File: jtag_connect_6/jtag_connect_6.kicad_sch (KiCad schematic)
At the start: 2 parts, among them J1 jtag-connect-6, J2 Conn_01x06_Pin

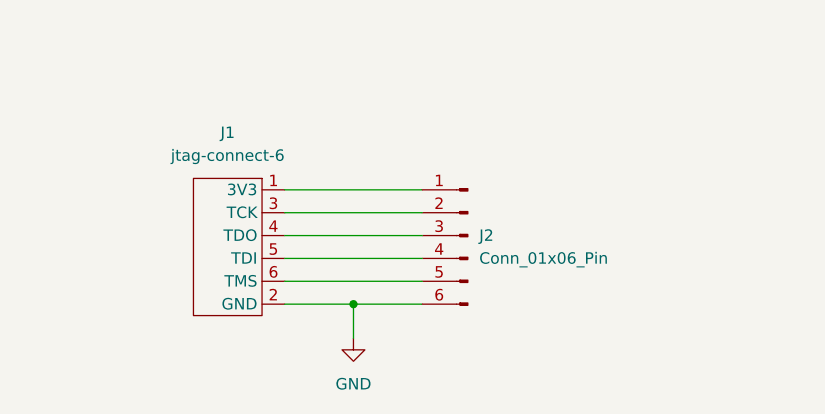
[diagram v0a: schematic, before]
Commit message: Better size and new pins for JTAG
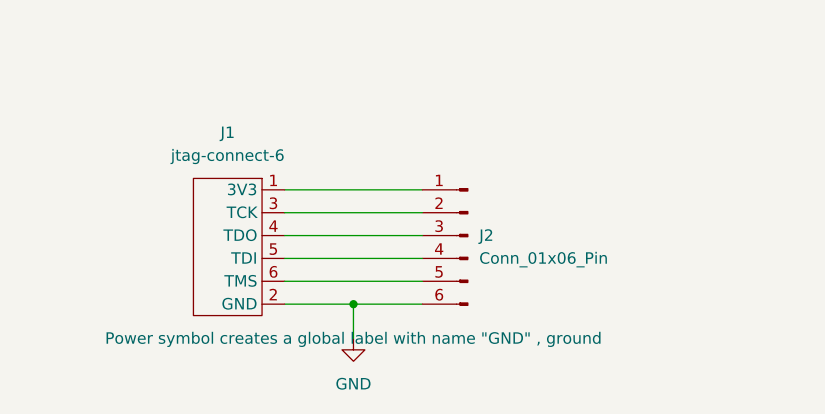
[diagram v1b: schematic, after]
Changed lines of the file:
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@@
 			)
 		)
-		(property "Description" ""
+		(property "Description" "Power symbol creates a global label with name \"GND\" , ground"
 			(at 113.03 105.41 0)
 			(effects

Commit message: Update JTAG to use plated through holes for strength. Also use Sipeed RV Debugger pinout
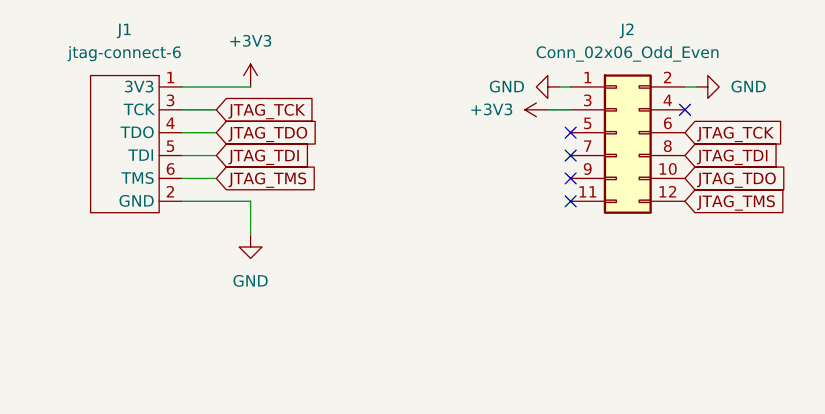
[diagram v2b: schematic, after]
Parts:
- removed J2: Conn_01x06_Pin, Connector_PinHeader_2.54mm:PinHeader_1x06_P2.54mm_Vertical, symbol Connector:Conn_01x06_Pin
- added J2: Conn_02x06_Odd_Even, Connector_PinSocket_2.54mm:PinSocket_2x06_P2.54mm_Vertical, symbol Connector_Generic:Conn_02x06_Odd_Even
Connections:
- net GND: now also J2.1 (Pin_1), J2.2 (Pin_2)
- net +3V3: now reaches J1.1 (3V3)
- net +3V3: now also J2.3 (Pin_3)
- net JTAG_TCK: now reaches J1.3 (TCK)
- net JTAG_TCK: now also J2.6 (Pin_6)
- net JTAG_TDO: now reaches J1.4 (TDO)
- net JTAG_TDO: now also J2.10 (Pin_10)
- net JTAG_TDI: now reaches J1.5 (TDI)
- net JTAG_TDI: now also J2.8 (Pin_8)
- net JTAG_TMS: now reaches J1.6 (TMS)
- net JTAG_TMS: now also J2.12 (Pin_12)
- no-connect marks 0 -> 5
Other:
- moved on the sheet: J1
